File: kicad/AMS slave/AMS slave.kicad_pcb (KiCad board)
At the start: 2 copper layers, 68 x 95 mm, 111 parts, among them J1 Conn_02x08_Top_Bottom, J2 Conn_01x04, J3 Conn_02x03_Odd_Even, Q1 2N7002, Q2 AO3400A, Q3 AO3401A, SW1 SW_Push, SW2 SW_Push, U1 BQ76940DBT, U2 ATmega328P-A, U3 MCP2515-xST, U4 ISO1050DUB, Y1 Crystal, Y2 8MHz

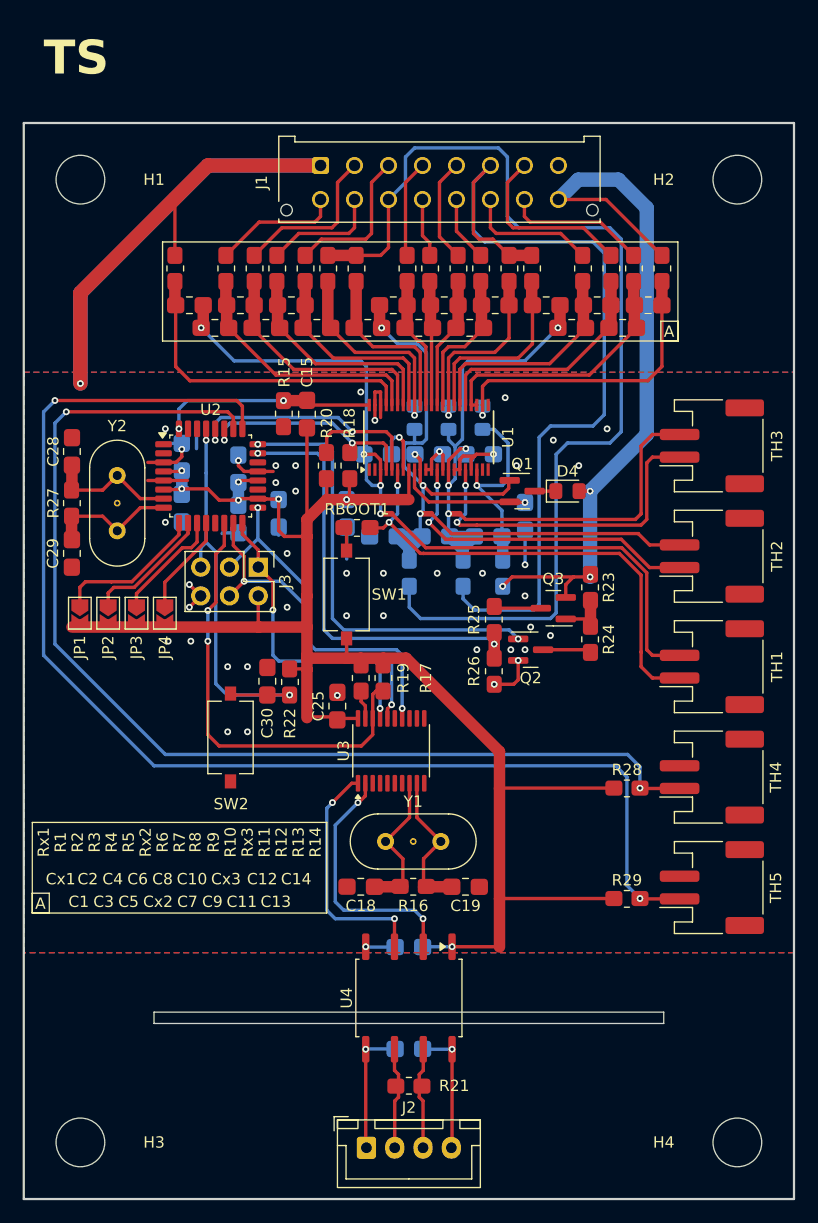
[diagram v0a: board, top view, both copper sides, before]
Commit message: AMS slave schem 0.4.3, pcb 0.4.4
schematic: switched out thermistors for 1x02 MP connector symbols, fixed mangled annotations
PCB: switched out thermistor connectors for the correct type
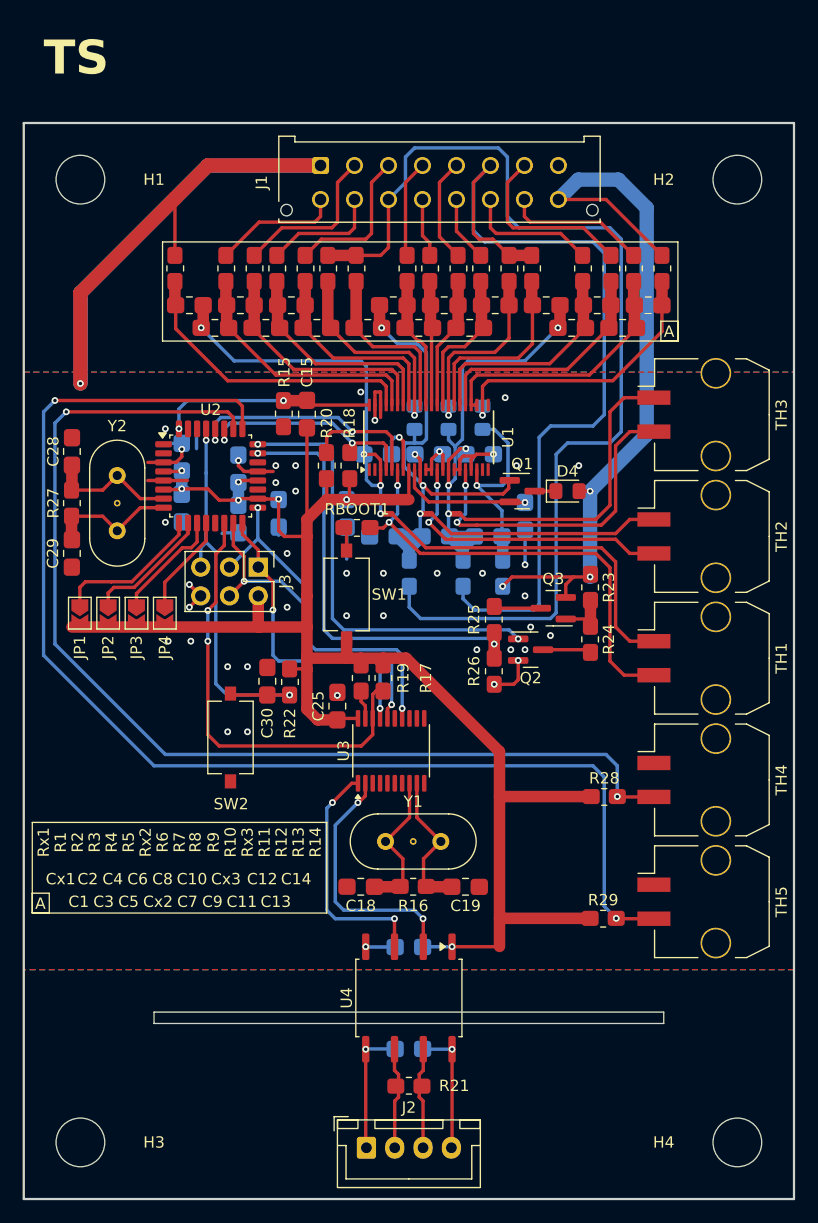
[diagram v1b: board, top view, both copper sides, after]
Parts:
- Q1: value 2N7002 -> KY2N7002
- Q2: value AO3400A -> AO3402
- Q3: value AO3401A -> NCE60P04Y
- TH1, TH2, TH3, TH4, TH5: value Thermistor -> Conn_01x02_MountingPin; footprint Connector_JST:JST_PH_S2B-PH-SM4-TB_1x02-1MP_P2.00mm_Horizontal -> Connector_Molex:Molex_Micro-Fit_3.0_43650-0210_1x02-1MP_P3.00mm_Horizontal
- Y1: value Crystal -> 20MHz
- moved TH3 2.75 mm to (85.8, 50.8), turned to -90 degrees
- moved R29 2.73 mm to (76.2, 95.2)
- moved R28 2.14 mm to (76.2, 84.5)
- moved TH2 1.75 mm to (85.8, 61.5), turned to -90 degrees
- moved TH5 1.25 mm to (85.8, 93.8), turned to -90 degrees
- moved TH1 0.75 mm to (85.8, 72.2), turned to -90 degrees
- moved TH4 0.25 mm to (85.8, 83.0), turned to -90 degrees
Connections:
- net /AMS slave 1/ALERT renamed /ALERT
- net /AMS slave 1/CANH renamed /CANH
- net /AMS slave 1/CANL renamed /CANL
- net /AMS slave 1/MISO renamed /MISO
- net /AMS slave 1/MOSI renamed /MOSI
- net /AMS slave 1/RST renamed /RST
- net /AMS slave 1/SCK renamed /SCK
- net /AMS slave 1/SCL renamed /SCL
- net /AMS slave 1/SDA renamed /SDA
- net /AMS slave 1/SS renamed /SS
- net /AMS slave 1/STACK_READ renamed /STACK_READ
- net /AMS slave 1/STACK_VALUE renamed /STACK_VALUE
- net /AMS slave 1/XTAL1 renamed /XTAL1
- net /AMS slave 1/XTAL2 renamed /XTAL2
- net /AMS slave 1/cell monitoring/BAT renamed /cell monitoring/BAT
- net /AMS slave 1/cell monitoring/VC0 renamed /cell monitoring/VC0
- net /AMS slave 1/cell monitoring/VC1 renamed /cell monitoring/VC1
- net /AMS slave 1/cell monitoring/VC10 renamed /cell monitoring/VC10
- net /AMS slave 1/cell monitoring/VC10B renamed /cell monitoring/VC10B
- net /AMS slave 1/cell monitoring/VC10X renamed /cell monitoring/VC10X
- net /AMS slave 1/cell monitoring/VC11 renamed /cell monitoring/VC11
- net /AMS slave 1/cell monitoring/VC12 renamed /cell monitoring/VC12
- net /AMS slave 1/cell monitoring/VC13 renamed /cell monitoring/VC13
- net /AMS slave 1/cell monitoring/VC15 renamed /cell monitoring/VC15
- net /AMS slave 1/cell monitoring/VC2 renamed /cell monitoring/VC2
- net /AMS slave 1/cell monitoring/VC3 renamed /cell monitoring/VC3
- net /AMS slave 1/cell monitoring/VC4 renamed /cell monitoring/VC4
- net /AMS slave 1/cell monitoring/VC5 renamed /cell monitoring/VC5
- net /AMS slave 1/cell monitoring/VC5B renamed /cell monitoring/VC5B
- net /AMS slave 1/cell monitoring/VC5X renamed /cell monitoring/VC5X
- net /AMS slave 1/cell monitoring/VC6 renamed /cell monitoring/VC6
- net /AMS slave 1/cell monitoring/VC7 renamed /cell monitoring/VC7
- net /AMS slave 1/cell monitoring/VC8 renamed /cell monitoring/VC8
- net /AMS slave 1/cell monitoring/VC9 renamed /cell monitoring/VC9
- net /AMS slave 1/cell monitoring/cell 1 renamed /cell monitoring/cell 1
- net /AMS slave 1/cell monitoring/cell 10 renamed /cell monitoring/cell 10
- net /AMS slave 1/cell monitoring/cell 11 renamed /cell monitoring/cell 11
- net /AMS slave 1/cell monitoring/cell 12 renamed /cell monitoring/cell 12
- net /AMS slave 1/cell monitoring/cell 13 renamed /cell monitoring/cell 13
- net /AMS slave 1/cell monitoring/cell 2 renamed /cell monitoring/cell 2
- net /AMS slave 1/cell monitoring/cell 3 renamed /cell monitoring/cell 3
- net /AMS slave 1/cell monitoring/cell 4 renamed /cell monitoring/cell 4
- net /AMS slave 1/cell monitoring/cell 5 renamed /cell monitoring/cell 5
- net /AMS slave 1/cell monitoring/cell 6 renamed /cell monitoring/cell 6
- net /AMS slave 1/cell monitoring/cell 7 renamed /cell monitoring/cell 7
- net /AMS slave 1/cell monitoring/cell 8 renamed /cell monitoring/cell 8
- net /AMS slave 1/cell monitoring/cell 9 renamed /cell monitoring/cell 9
- NT1 pad 1: /AMS slave 1/cell monitoring/TS1- -> /cell monitoring/TS1-
- NT2 pad 1: /AMS slave 1/cell monitoring/TS2- -> /cell monitoring/TS2-
- NT3 pad 1: /AMS slave 1/cell monitoring/TS3- -> /cell monitoring/TS3-
- R28 pad 2: /AMS slave 1/TS4+ -> /TS4+
- R29 pad 2: /AMS slave 1/TS5+ -> /TS5+
- RBOOT1 pad 2: /AMS slave 1/cell monitoring/TS1+ -> /cell monitoring/TS1+
- TH1 pad 1: /AMS slave 1/cell monitoring/TS1+ -> /cell monitoring/TS1-
- TH1 pad 2: /AMS slave 1/cell monitoring/TS1- -> /cell monitoring/TS1+
- TH1 pad MP: (no net) -> GND
- TH2 pad 1: /AMS slave 1/cell monitoring/TS2+ -> /cell monitoring/TS2-
- TH2 pad 2: /AMS slave 1/cell monitoring/TS2- -> /cell monitoring/TS2+
- TH2 pad MP: (no net) -> GND
- TH3 pad 1: /AMS slave 1/cell monitoring/TS3+ -> /cell monitoring/TS3-
- TH3 pad 2: /AMS slave 1/cell monitoring/TS3- -> /cell monitoring/TS3+
- TH3 pad MP: (no net) -> GND
- TH4 pad 1: /AMS slave 1/TS4+ -> GND
- TH4 pad 2: GND -> /TS4+
- TH4 pad MP: (no net) -> GND
- TH5 pad 1: /AMS slave 1/TS5+ -> GND
- TH5 pad 2: GND -> /TS5+
- TH5 pad MP: (no net) -> GND
- U1 pad 13: /AMS slave 1/cell monitoring/TS2+ -> /cell monitoring/TS2+
- U1 pad 18: /AMS slave 1/cell monitoring/TS3+ -> /cell monitoring/TS3+
- U1 pad 6: /AMS slave 1/cell monitoring/TS1+ -> /cell monitoring/TS1+
- U2 pad 25: /AMS slave 1/TS5+ -> /TS5+
- U2 pad 26: /AMS slave 1/TS4+ -> /TS4+
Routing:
- net /AMS slave 1/TS5+: track 112.3 -> 0.00 mm, vias 2 -> 0
- net /TS5+: track 0.00 -> 111.9 mm, vias 0 -> 2
- net /AMS slave 1/TS4+: track 98.4 -> 0.00 mm, vias 2 -> 0
- net /TS4+: track 0.00 -> 96.9 mm, vias 0 -> 2
- net /AMS slave 1/cell monitoring/TS1+: track 43.2 -> 0.00 mm, vias 2 -> 0
- net /cell monitoring/TS1+: track 0.00 -> 40.9 mm, vias 0 -> 2
- net /AMS slave 1/cell monitoring/TS1-: track 34.6 -> 0.00 mm
- net /cell monitoring/TS1-: track 0.00 -> 31.2 mm
- net /AMS slave 1/cell monitoring/TS3+: track 30.1 -> 0.00 mm, vias 2 -> 0
- net /cell monitoring/TS3+: track 0.00 -> 29.2 mm, vias 0 -> 2
- net /AMS slave 1/cell monitoring/TS2+: track 28.8 -> 0.00 mm, vias 2 -> 0
- net /cell monitoring/TS3-: track 0.00 -> 26.6 mm
- net /AMS slave 1/cell monitoring/TS3-: track 26.2 -> 0.00 mm
- net /cell monitoring/TS2+: track 0.00 -> 26.0 mm, vias 0 -> 2
- net /AMS slave 1/cell monitoring/TS2-: track 23.0 -> 0.00 mm
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
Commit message: AMS slave schem 0.4.4 pcb 0.5.0
schematic cleaned up with labels and removed clipping text
new PCB iteration, with generally shorter traces where applicable, better filter capacitor layout, and pinout labels with silkscreen
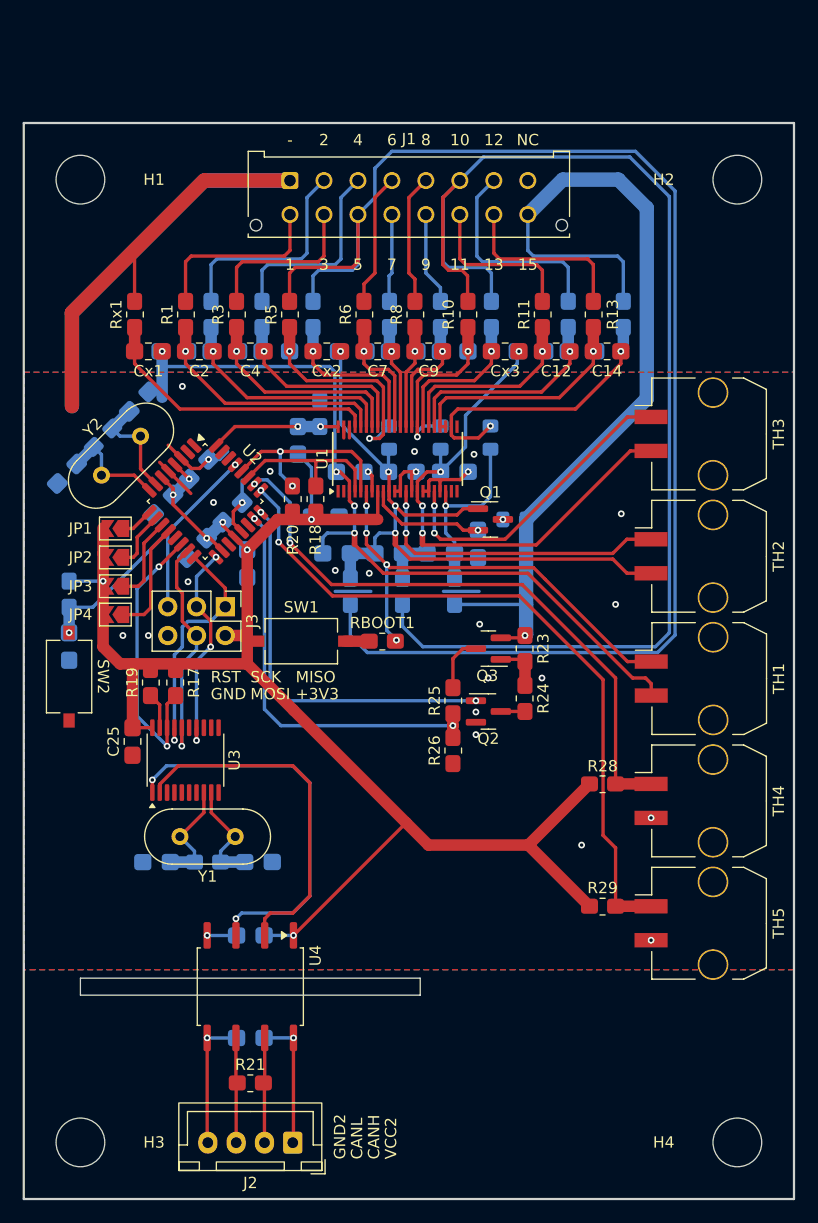
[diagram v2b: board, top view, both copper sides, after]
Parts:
- removed ? (x2): , 
- C1, C10, C11, C13, C15, C18, C19, C28, C29, C3, C30, C5, C6, C8, D4, R12, R14, R15, R16, R2, R22, R27, R4, R7, R9, Rx2, Rx3: moved to B.Cu
- moved R22 21.0 mm to (29.0, 66.6)
- moved R19 18.5 mm to (36.2, 74.4), turned to 90 degrees
- moved C19 18.4 mm to (45.7, 90.2), turned to 0 degrees
- moved R17 18.4 mm to (38.4, 74.4), turned to -90 degrees
- moved C25 18.3 mm to (34.6, 79.6), turned to 90 degrees
- moved R16 18.3 mm to (41.2, 90.2)
- moved U3 18.2 mm to (39.3, 81.2)
- moved C18 18.2 mm to (36.7, 90.2)
- moved C30 17.8 mm to (29.0, 71.2), turned to 90 degrees
- moved SW2 15.2 mm to (29.0, 73.9)
- moved C26 14.0 mm to (45.0, 96.7)
- moved U4 14.0 mm to (45.0, 101.2)
- moved C27 14.0 mm to (45.0, 105.8)
- moved R21 14.0 mm to (45.0, 109.8), turned to 0 degrees
- moved Y1 13.3 mm to (43.7, 88.0), turned to 180 degrees
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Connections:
- C18 pad 2: Net-(U3-OSC2) -> /XTAL_MCP1
- C19 pad 1: GND -> /XTAL_MCP2
- C19 pad 2: Net-(U3-OSC1) -> GND
- C29 pad 1: GND -> /XTAL2
- C29 pad 2: /XTAL2 -> GND
- J2 pad 1: GND2 -> VCC2
- J2 pad 2: /CANL -> /CANH
- J2 pad 3: /CANH -> /CANL
- J2 pad 4: VCC2 -> GND2
- R16 pad 1: Net-(U3-OSC2) -> /XTAL_MCP1
- R16 pad 2: Net-(U3-OSC1) -> /XTAL_MCP2
- R17 pad 1: /SS -> +3V3
- R17 pad 2: +3V3 -> /SS
- R19 pad 1: +3V3 -> Net-(U3-~{RESET})
- R19 pad 2: Net-(U3-~{RESET}) -> +3V3
- R21 pad 1: /CANH -> /CANL
- R21 pad 2: /CANL -> /CANH
- R25 pad 1: Net-(Q3-D) -> /STACK_VALUE
- R25 pad 2: /STACK_VALUE -> Net-(Q3-D)
- R26 pad 1: /STACK_VALUE -> GND
- R26 pad 2: GND -> /STACK_VALUE
- R27 pad 1: /XTAL2 -> /XTAL1
- R27 pad 2: /XTAL1 -> /XTAL2
- SW1 pad 1: Net-(RBOOT1-Pad1) -> +3V3
- SW1 pad 2: +3V3 -> Net-(RBOOT1-Pad1)
- TH1 pad 1: /cell monitoring/TS1- -> /cell monitoring/TS1+
- TH1 pad 2: /cell monitoring/TS1+ -> /cell monitoring/TS1-
- TH2 pad 1: /cell monitoring/TS2- -> /cell monitoring/TS2+
- TH2 pad 2: /cell monitoring/TS2+ -> /cell monitoring/TS2-
- TH3 pad 1: /cell monitoring/TS3- -> /cell monitoring/TS3+
- TH3 pad 2: /cell monitoring/TS3+ -> /cell monitoring/TS3-
- TH4 pad 1: GND -> /TS4+
- TH4 pad 2: /TS4+ -> GND
- TH5 pad 1: GND -> /TS5+
- TH5 pad 2: /TS5+ -> GND
- U3 pad 8: Net-(U3-OSC2) -> /XTAL_MCP1
- U3 pad 9: Net-(U3-OSC1) -> /XTAL_MCP2
- Y1 pad 1: Net-(U3-OSC2) -> /XTAL_MCP2
- Y1 pad 2: Net-(U3-OSC1) -> /XTAL_MCP1
- Y2 pad 1: /XTAL1 -> /XTAL2
- Y2 pad 2: /XTAL2 -> /XTAL1
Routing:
- net /TS5+: track 111.9 -> 62.5 mm
- net /TS4+: track 96.9 -> 53.9 mm
- net /cell monitoring/cell 10: track 75.3 -> 113.9 mm
- net /cell monitoring/cell 5: track 93.1 -> 129.3 mm
- net /SS: track 39.2 -> 25.3 mm
- net Net-(U3-TXCAN): track 21.4 -> 35.0 mm
- net Net-(U3-OSC2): track 13.1 -> 0.00 mm
- net Net-(U3-OSC1): track 13.1 -> 0.00 mm
- net PACK+: track 66.5 -> 79.1 mm, vias 3 -> 1
- net /SCK: track 31.6 -> 19.1 mm, vias 2 -> 3
- net /cell monitoring/VC10X: track 41.5 -> 29.1 mm
- net GND: track 146.2 -> 135.0 mm, vias 45 -> 27
- net +3V3: track 159.6 -> 148.9 mm, vias 7 -> 8
- net Net-(JP1-A): track 13.2 -> 2.87 mm
- net /MOSI: track 30.9 -> 20.5 mm, vias 2 -> 1
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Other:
- outline, holes or cut-outs redrawn
- board text added: "+3V3"
- board text added: "-"
- board text added: "1"
- board text added: "10"
- board text added: "11"
- board text added: "12"
- board text added: "13"
- board text added: "15"
- board text added: "2"
- board text added: "3"
- board text added: "4"
- board text added: "5"
- board text added: "6"
- board text added: "7"
- board text added: "8"
- board text added: "9"
- board text added: "CANH"
- board text added: "CANL"
- board text added: "GND"
- board text added: "GND2"
- board text added: "MISO"
- board text added: "MOSI"
- board text added: "NC"
- board text added: "RST"
- board text added: "SCK"
- board text added: "VCC2"
- board text removed: "A"
- board text removed: "TS"

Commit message: AMS slave schem 0.4.5 PCB 0.5.1
PCB: Thermistor connector footprint changed
Adjusted ground traces and other trace position
Schematic: updated thermistor connector symbol
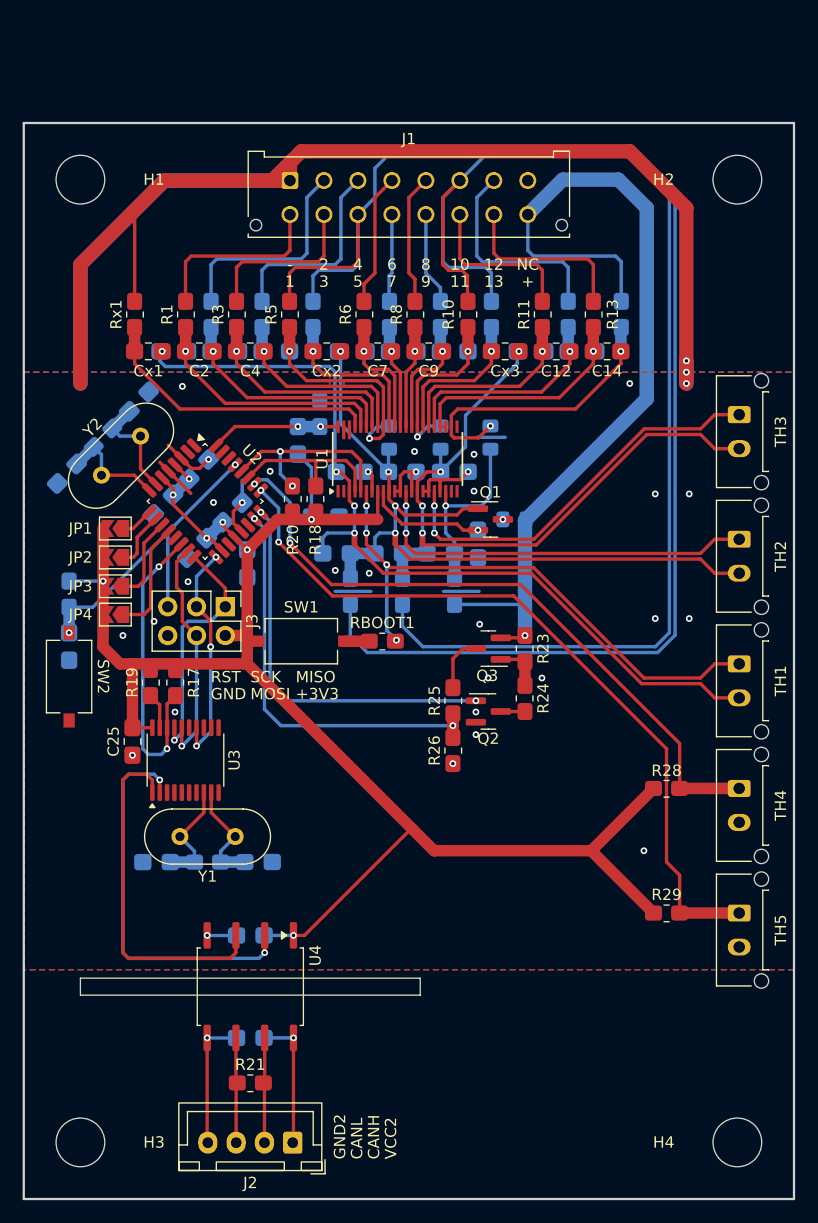
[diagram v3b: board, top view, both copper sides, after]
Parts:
- TH1, TH2, TH3, TH4, TH5: footprint Connector_Molex:Molex_Micro-Fit_3.0_43650-0210_1x02-1MP_P3.00mm_Horizontal -> Connector_Molex:Molex_Micro-Fit_3.0_43650-0215_1x02_P3.00mm_Vertical
- moved R29 5.68 mm to (81.8, 94.8)
- moved R28 5.67 mm to (81.8, 83.8)
- moved TH3 3.16 mm to (88.2, 50.8)
- moved TH2 3.06 mm to (88.2, 61.8)
- moved TH1 2.95 mm to (88.2, 72.8)
- moved TH4 2.88 mm to (88.2, 83.8)
- moved TH5 2.81 mm to (88.2, 94.8)
- moved R14 0.18 mm to (77.7, 41.9)
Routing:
- net GND: track 135.0 -> 194.5 mm, vias 27 -> 35
- net /cell monitoring/TS3-: track 23.6 -> 32.5 mm
- net /cell monitoring/TS1+: track 41.1 -> 50.0 mm
- net /cell monitoring/TS3+: track 27.5 -> 35.4 mm
- net /cell monitoring/TS2-: track 23.6 -> 31.4 mm
- net /cell monitoring/TS2+: track 27.2 -> 35.0 mm
- net /cell monitoring/TS1-: track 32.3 -> 39.6 mm
- net +3V3: track 148.9 -> 155.3 mm
- net /TS4+: track 53.9 -> 58.7 mm
- net /TS5+: track 62.5 -> 67.3 mm
- net Net-(U3-TXCAN): track 35.0 -> 31.3 mm, vias 2 -> 0
- net Net-(U3-RXCAN): track 31.6 -> 34.5 mm, vias 0 -> 2
- net /SS: track 25.3 -> 27.0 mm
- net /SCK: track 19.1 -> 20.1 mm
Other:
- board text added: "+"
- board text removed: "15"
